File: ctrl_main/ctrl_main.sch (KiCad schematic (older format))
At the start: 19 parts, among them IC1 SN74HC125N, J1 B2B-XH-A(LF)(SN), J2 B2B-XH-A(LF)(SN), J3 B2B-XH-A(LF)(SN), P11 CONN_01X03, P12 CONN_01X03, P4 CONN_01X04, P5 CONN_01X04, P6 CONN_01X04, P7 CONN_01X04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

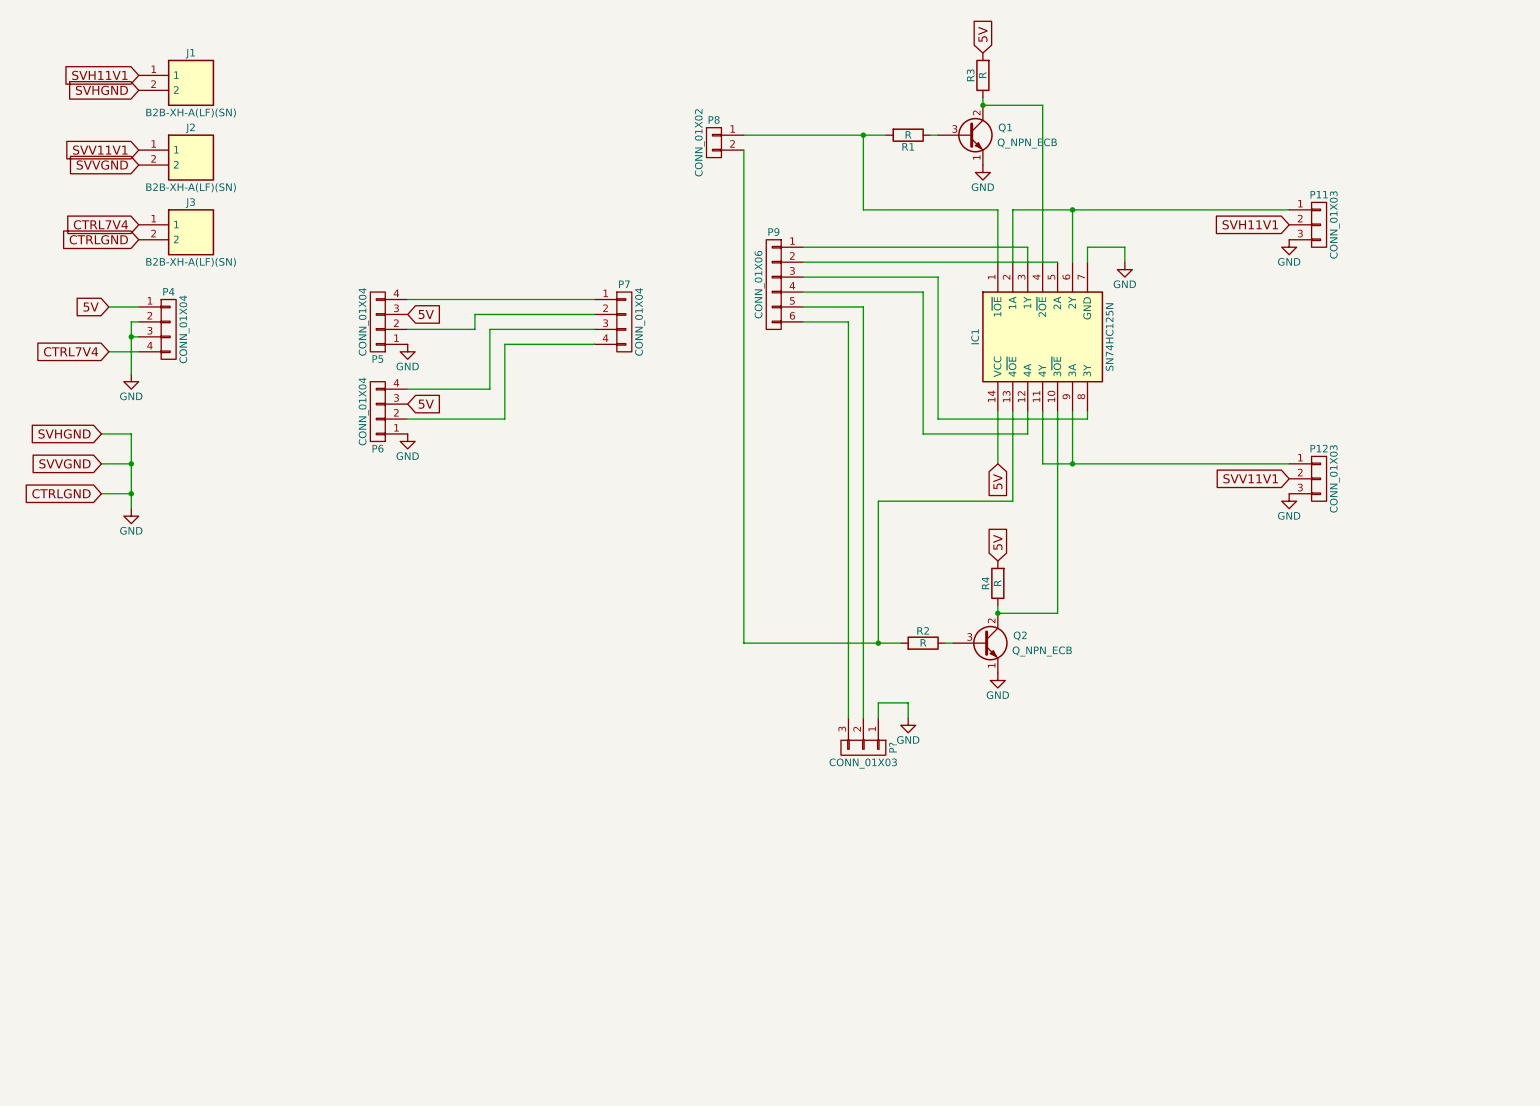
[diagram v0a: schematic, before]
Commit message: CTRL7V4->Vin Rev2.1
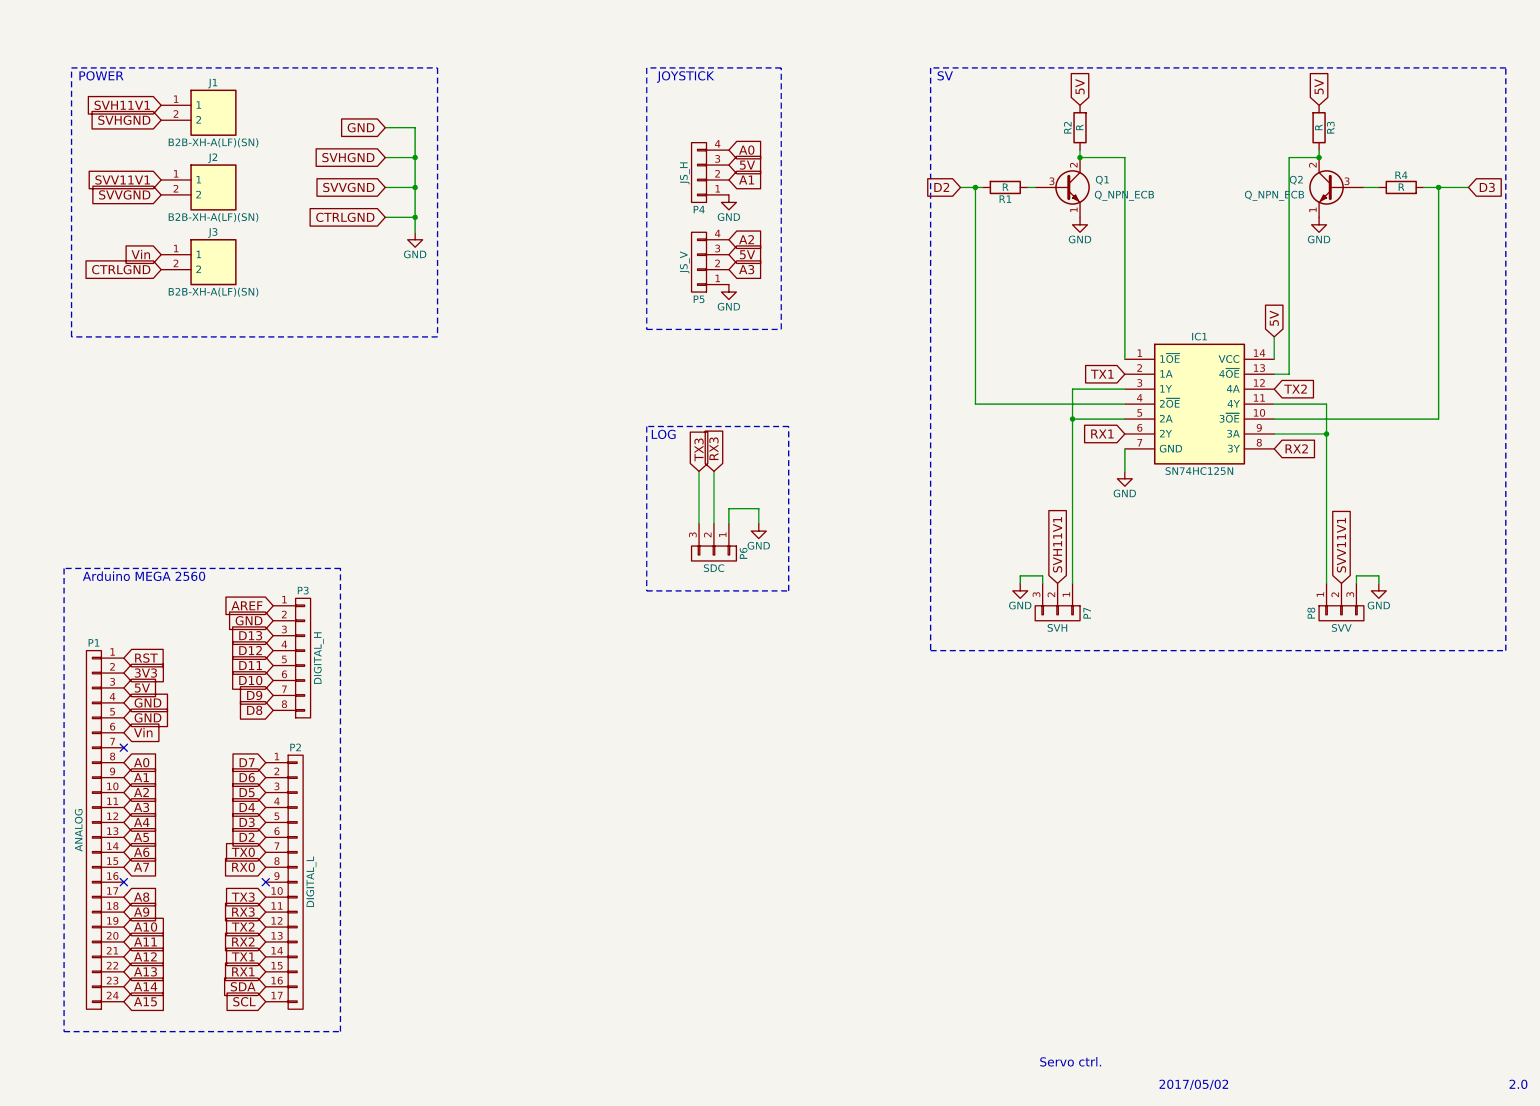
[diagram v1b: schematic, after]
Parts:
- removed P4, P7: CONN_01X04, Pin_Headers:Pin_Header_Straight_1x04_Pitch1.27mm, symbol CONN_01X04
- removed P8: CONN_01X02, Pin_Headers:Pin_Header_Straight_1x02_Pitch1.27mm, symbol CONN_01X02
- removed P9: CONN_01X06, Pin_Headers:Pin_Header_Straight_1x06_Pitch1.27mm, symbol CONN_01X06
- added P1: ANALOG, Pin_Headers:Pin_Header_Straight_1x24_Pitch2.54mm, symbol CONN_01X24
- added P2: DIGITAL_L, Pin_Headers:Pin_Header_Straight_1x17_Pitch2.54mm, symbol CONN_01X17
- added P3: DIGITAL_H, Pin_Headers:Pin_Header_Straight_1x08_Pitch2.54mm, symbol CONN_01X08
- J1, J2, J3: footprint Pin_Headers:Pin_Header_Straight_1x02_Pitch1.27mm -> Pin_Headers:Pin_Header_Straight_1x02_Pitch2.54mm
- P4: renamed from P5; value CONN_01X04 -> JS_H; footprint Pin_Headers:Pin_Header_Straight_1x04_Pitch1.27mm -> Pin_Headers:Pin_Header_Straight_1x04_Pitch2.54mm
- P5: renamed from P6; value CONN_01X04 -> JS_V; footprint Pin_Headers:Pin_Header_Straight_1x04_Pitch1.27mm -> Pin_Headers:Pin_Header_Straight_1x04_Pitch2.54mm
- P6: renamed from P?; value CONN_01X03 -> SDC; footprint (none) -> Pin_Headers:Pin_Header_Straight_1x03_Pitch2.54mm
- P7: renamed from P11; value CONN_01X03 -> SVH; footprint Pin_Headers:Pin_Header_Straight_1x03_Pitch1.27mm -> Pin_Headers:Pin_Header_Straight_1x03_Pitch2.54mm
- P8: renamed from P12; value CONN_01X03 -> SVV; footprint Pin_Headers:Pin_Header_Straight_1x03_Pitch1.27mm -> Pin_Headers:Pin_Header_Straight_1x03_Pitch2.54mm
- renumbered R3 to R2, R4 to R3, R2 to R4
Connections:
- net 5V: now also P1.3 (P3)
- net GND: now also P1.4 (P4), P1.5 (P5), P3.2 (P2)
- net A1: now reaches P4.2 (P2)
- net A1: now also P1.9 (P9)
- net A0: now reaches P4.4 (P4)
- net A0: now also P1.8 (P8)
- net A3: now reaches P5.2 (P2)
- net A3: now also P1.11 (P11)
- net A2: now reaches P5.4 (P4)
- net A2: now also P1.10 (P10)
- net at IC1.1 (1~OE): now also Q1.2 (C), R2.1; no longer R1.2
- net at Q2.2 (C), R3.1: now also IC1.13 (4~OE); no longer IC1.10 (3~OE)
- net TX2: now reaches IC1.12 (4A)
- net TX2: now also P2.12 (P12)
- net D3: now reaches R4.2
- net D3: now also IC1.10 (3~OE), P2.5 (P5); no longer IC1.13 (4~OE)
- net at IC1.3 (1Y): now also IC1.5 (2A), P7.1 (P1)
- net RX2: now reaches IC1.8 (3Y)
- net RX2: now also P2.13 (P13)
- net RX3: now reaches P6.2 (P2)
- net RX3: now also P2.11 (P11)
- net TX3: now reaches P6.3 (P3)
- net TX3: now also P2.10 (P10)
- net CTRL7V4 renamed Vin
- net Vin: now also P1.6 (P6)
- new net 3V3: P1.2 (P2)
- new net A10: P1.19 (P19)
- new net A11: P1.20 (P20)
- new net A12: P1.21 (P21)
- new net A13: P1.22 (P22)
- new net A14: P1.23 (P23)
- new net A15: P1.24 (P24)
- new net A4: P1.12 (P12)
- new net A5: P1.13 (P13)
- new net A6: P1.14 (P14)
- new net A7: P1.15 (P15)
- new net A8: P1.17 (P17)
- new net A9: P1.18 (P18)
- new net AREF: P3.1 (P1)
- new net D10: P3.6 (P6)
- new net D11: P3.5 (P5)
- new net D12: P3.4 (P4)
- new net D13: P3.3 (P3)
- new net D2: IC1.4 (2~OE), P2.6 (P6), R1.2
- new net D4: P2.4 (P4)
- new net D5: P2.3 (P3)
- new net D6: P2.2 (P2)
- new net D7: P2.1 (P1)
- new net D8: P3.8 (P8)
- new net D9: P3.7 (P7)
- new net RST: P1.1 (P1)
- new net RX0: P2.8 (P8)
- new net RX1: IC1.6 (2Y), P2.15 (P15)
- new net SCL: P2.17 (P17)
- new net SDA: P2.16 (P16)
- new net TX0: P2.7 (P7)
- new net TX1: IC1.2 (1A), P2.14 (P14)
- no-connect marks 0 -> 3
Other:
- note added: "2.0"
- note added: "2017/05/02"
- note added: "Arduino MEGA 2560"
- note added: "JOYSTICK"
- note added: "LOG"
- note added: "POWER"
- note added: "SV"
- note added: "Servo ctrl."
- moved on the sheet: J1, J2, J3, P4, P5, P6, P7, P8, Q1, Q2, R1, R2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

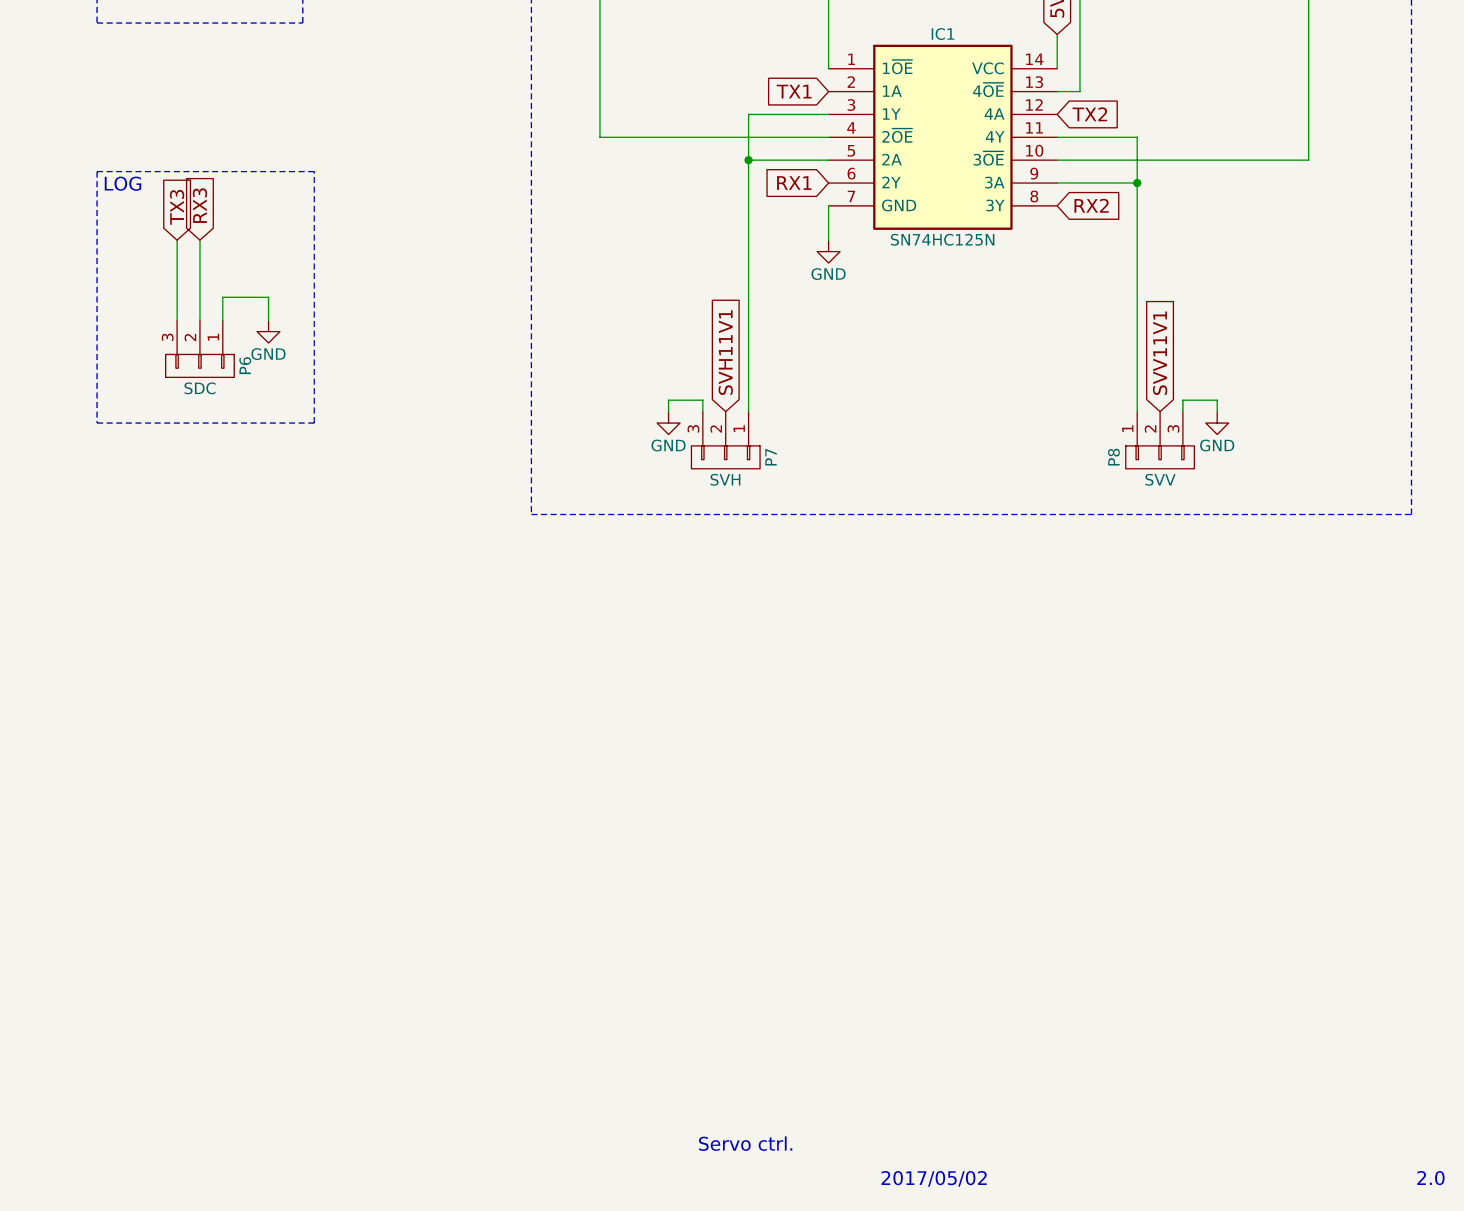
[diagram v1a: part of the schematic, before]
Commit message: P6のRXとTX入れ替え。フットプリントの配置と配線完了
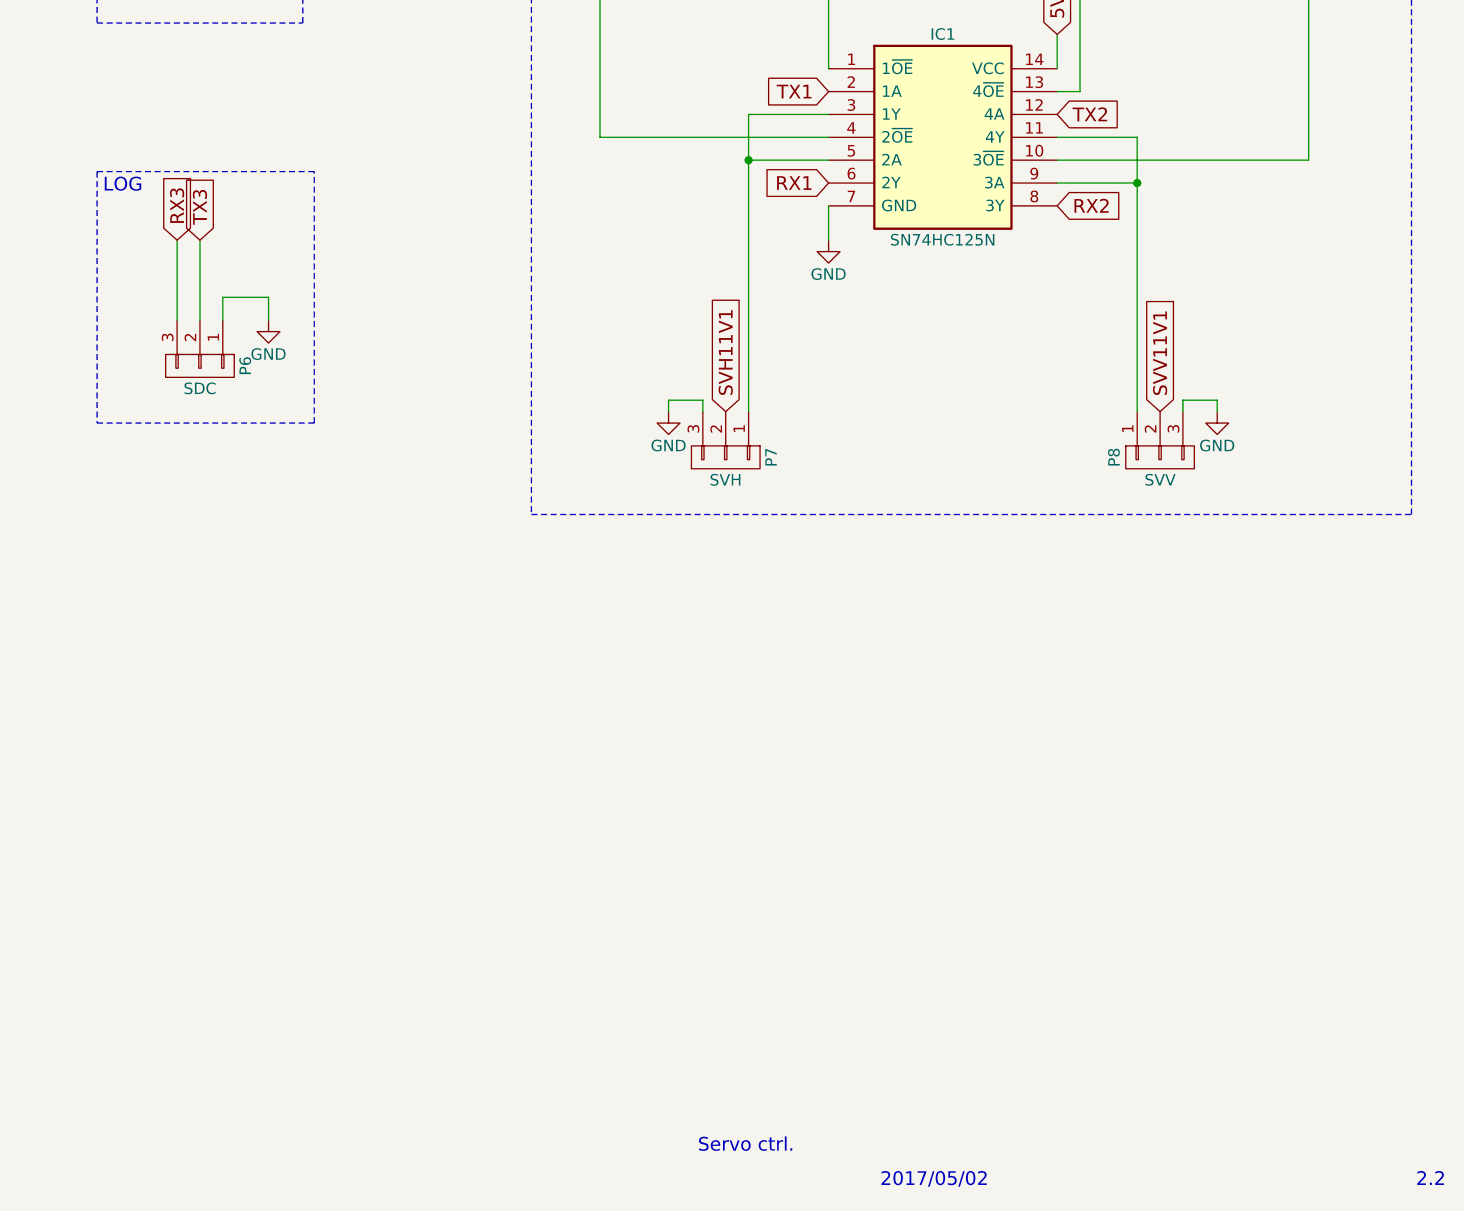
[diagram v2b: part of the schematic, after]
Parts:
- R1: footprint Resistors_ThroughHole:R_Axial_DIN0204_L3.6mm_D1.6mm_P2.54mm_Vertical -> Resistors_ThroughHole:R_Axial_DIN0204_L3.6mm_D1.6mm_P5.08mm_Horizontal
- R4: footprint Resistors_ThroughHole:R_Axial_DIN0204_L3.6mm_D1.6mm_P2.54mm_Vertical -> Resistors_ThroughHole:R_Axial_DIN0204_L3.6mm_D1.6mm_P7.62mm_Horizontal
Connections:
- net RX3: now also P6.3 (P3); no longer P6.2 (P2)
- net TX3: now also P6.2 (P2); no longer P6.3 (P3)
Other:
- note added: "2.2"
- note removed: "2.0"
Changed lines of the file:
@@
 F 0 "R1" V 7280 1600 50  0000 C CNN
 F 1 "R" V 7200 1600 50  0000 C CNN
-F 2 "Resistors_ThroughHole:R_Axial_DIN0204_L3.6mm_D1.6mm_P2.54mm_Vertical" V 7130 1600 50  0001 C CNN
+F 2 "Resistors_ThroughHole:R_Axial_DIN0204_L3.6mm_D1.6mm_P5.08mm_Horizontal" V 7130 1600 50  0001 C CNN
 F 3 "" H 7200 1600 50  0000 C CNN
 	1    7200 1600
@@
 F 0 "R4" V 9930 1600 50  0000 C CNN
 F 1 "R" V 9850 1600 50  0000 C CNN
-F 2 "Resistors_ThroughHole:R_Axial_DIN0204_L3.6mm_D1.6mm_P2.54mm_Vertical" V 9780 1600 50  0001 C CNN
+F 2 "Resistors_ThroughHole:R_Axial_DIN0204_L3.6mm_D1.6mm_P7.62mm_Horizontal" V 9780 1600 50  0001 C CNN
 F 3 "" H 9850 1600 50  0000 C CNN
 	1    9850 1600
@@
 Wire Wire Line
 	9700 4200 9700 4250
+Text GLabel 5150 3500 1    60   Input ~ 0
+RX3
 Text GLabel 5250 3500 1    60   Input ~ 0
-RX3
-Wire Wire Line
-	5250 3850 5250 3500
-Text GLabel 5150 3500 1    60   Input ~ 0
 TX3
-Wire Wire Line
-	5150 3850 5150 3500
 Text GLabel 5350 1350 2    60   Input ~ 0
 A0
@@
 Servo ctrl.
 Text Notes 10700 7650 2    60   ~ 0
-2.0
+2.2
 Text Notes 8700 7650 2    60   ~ 0
 2017/05/02
+Wire Wire Line
+	5150 3850 5150 3500
+Wire Wire Line
+	5250 3850 5250 3500
 $EndSCHEMATC
